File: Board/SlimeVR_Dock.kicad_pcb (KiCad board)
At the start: 2 copper layers, 83.8 x 76.8 mm, 91 parts, among them J1_Control1 Conn_01x03_Pin, J1_MainPW1 USB_C_Receptacle_USB2.0_16P, J1_Monitor1 Conn_01x03_Pin, J1_Prog1 Conn_01x03_Pin, J2 USB_C_Receptacle_USB2.0_16P, J3 USB_C_Receptacle_USB2.0_16P, J4 USB_C_Receptacle_USB2.0_16P, J5 USB_C_Receptacle_USB2.0_16P, J6 USB_C_Receptacle_USB2.0_16P, J7 USB_C_Receptacle_USB2.0_16P, J8 USB_C_Receptacle_USB2.0_16P, J9 USB_C_Receptacle_USB2.0_16P, Q1 AO3401A, Q2 BC857, Q3 BC857, Q4 BC857, Q5 BC857, U1 ESP32-C3-WROOM-02, U10 INA226, U11 AP22652W6-7, U12 INA226, U13 INA226, U14 AP22652W6-7, U15 INA226, U16 INA226, U17 74HC165, U18 74HC165, U19 74HC595, U2 CH224K, U3 XC6220B331MR, U5 AP22652W6-7, U6 INA226, U7 INA226, U8 AP22652W6-7, U9 INA226

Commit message: Updavení USB-C
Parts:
- removed JFan1: Conn_01x04_Pin, Connector:FanPinHeader_1x04_P2.54mm_Vertical
- added BZ1: Buzzer, Buzzer_Beeper:Buzzer_12x9.5RM7.6, F.Cu at (121.4, 72.0)
- added D1: 1N4148, Diode_SMD:D_0603_1608Metric, F.Cu at (134.4, 61.8)
- added J1Fan1: Conn_01x04_Pin, Connector:FanPinHeader_1x04_P2.54mm_Vertical, F.Cu at (124.9, 42.4)
- added J1Temp1: Conn_01x05_Pin, Connector_PinHeader_2.54mm:PinHeader_1x05_P2.54mm_Vertical, F.Cu at (124.9, 49.0)
- added Q6: BC817, Package_TO_SOT_SMD:SOT-23, F.Cu at (134.4, 72.2)
- added R33: 1k, Resistor_SMD:R_0603_1608Metric, F.Cu at (103.1, 85.6)
- moved J_FromR0 65.2 mm to (129.5, 49.0)
- moved J_ToR0 65.2 mm to (134.1, 49.0)
- moved U2 53.6 mm to (131.4, 57.3)
- moved C19 43.3 mm to (163.4, 61.8)
- moved R32 43.3 mm to (163.4, 78.7)
- moved C14 43.3 mm to (163.4, 47.3)
- moved C21 43.3 mm to (163.4, 76.2)
- moved J2 43.3 mm to (161.5, 43.2)
- moved J6 43.3 mm to (161.5, 57.6)
- moved R25 43.3 mm to (163.4, 49.8)
- moved R30 43.3 mm to (163.4, 64.3)
- moved U12 43.3 mm to (157.7, 62.8)
- moved U6 43.3 mm to (157.7, 48.4)
- moved J8 43.3 mm to (161.5, 72.1)
- moved U15 43.3 mm to (157.7, 77.2)
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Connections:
- U19 pad 4: unconnected-(U19-QE-Pad4) -> BZ
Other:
- board size 83.8 x 76.8 mm -> 82.8 x 69.8 mm

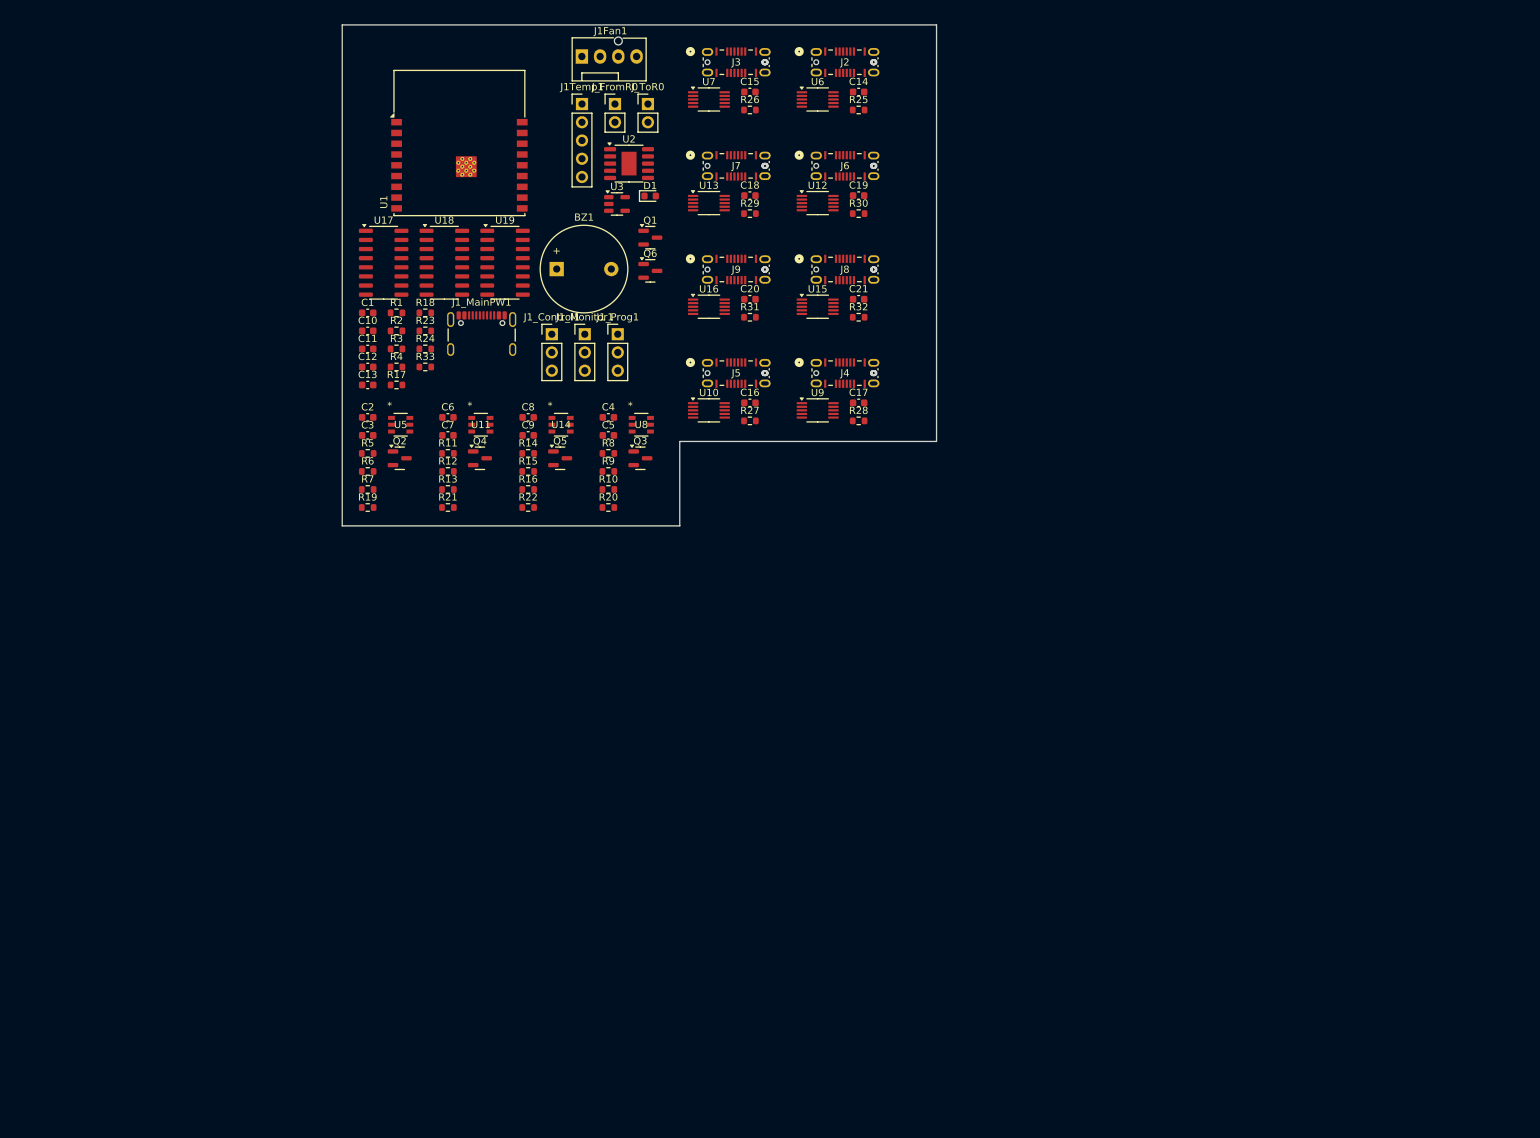
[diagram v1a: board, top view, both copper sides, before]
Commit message: layout
-bude asi potreba jiny footrpint usb-c
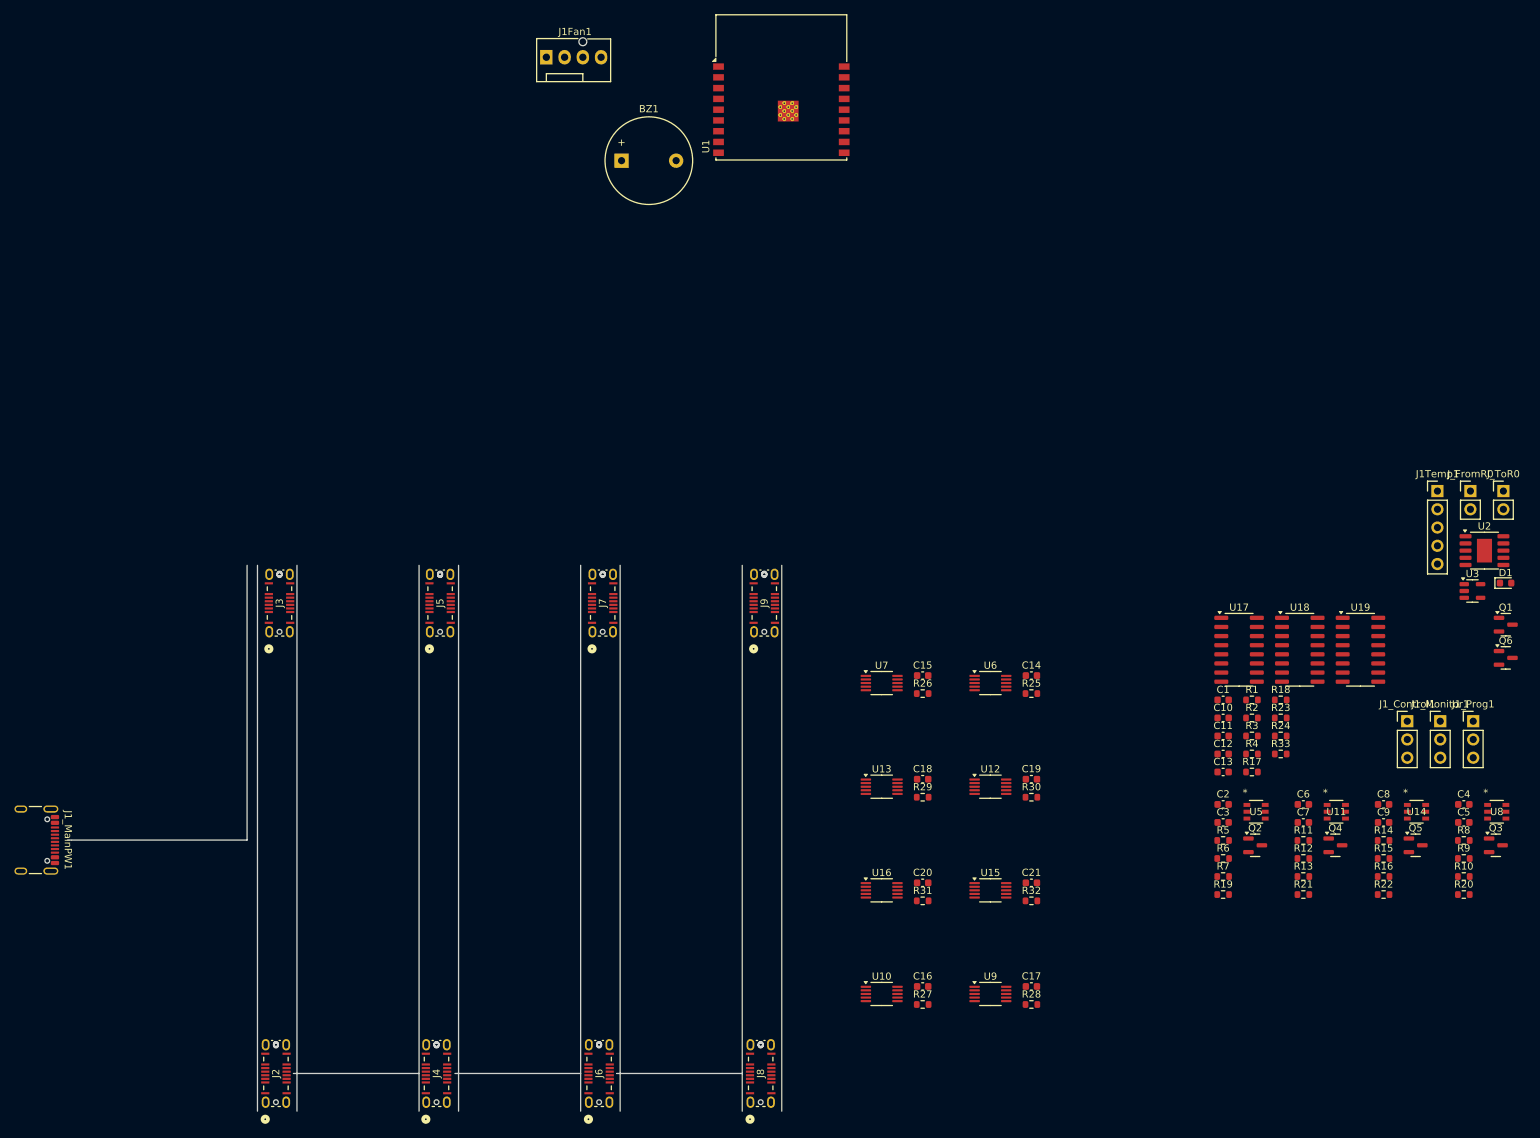
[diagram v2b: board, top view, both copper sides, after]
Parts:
- moved J2 161.6 mm to (82.3, 184.0), turned to 90 degrees
- moved J6 130.9 mm to (127.3, 184.0), turned to 90 degrees
- moved Q2 130.7 mm to (218.6, 152.2)
- moved Q5 130.7 mm to (241.0, 152.2)
- moved R18 130.7 mm to (222.2, 132.0)
- moved R23 130.7 mm to (222.2, 134.5)
- moved R24 130.7 mm to (222.2, 137.0)
- moved R33 130.7 mm to (222.2, 139.5)
- moved C1 130.7 mm to (214.2, 132.0)
- moved C10 130.7 mm to (214.2, 134.5)
- moved C11 130.7 mm to (214.2, 137.0)
- moved C12 130.7 mm to (214.2, 139.5)
- moved C13 130.7 mm to (214.2, 142.0)
- moved C2 130.7 mm to (214.2, 146.5)
- moved C3 130.7 mm to (214.2, 149.0)
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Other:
- board size 82.8 x 69.8 mm -> 99.4 x 76 mm

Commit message: minority upravy
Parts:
- added C22: 10uF, Capacitor_SMD:C_1210_3225Metric, F.Cu at (221.4, 37.4)
- added C23: 10uF, Capacitor_SMD:C_1210_3225Metric, F.Cu at (221.4, 41.6)
- added C24: 47uF, Capacitor_SMD:C_0805_2012Metric, F.Cu at (216.3, 36.8)
- added C25: 47uF, Capacitor_SMD:C_0805_2012Metric, F.Cu at (216.3, 39.8)
- added C26: 47uF, Capacitor_SMD:C_0805_2012Metric, F.Cu at (216.3, 42.8)
- added C27: 100nF, Capacitor_SMD:C_0805_2012Metric, F.Cu at (216.3, 45.8)
- added C28: 100nF, Capacitor_SMD:C_0805_2012Metric, F.Cu at (216.3, 48.8)
- added C29: 4.7uF, Capacitor_SMD:C_0805_2012Metric, F.Cu at (216.3, 51.8)
- added C30: 10uF, Capacitor_SMD:C_1210_3225Metric, F.Cu at (221.4, 45.9)
- added L1: 2.2uH, Inductor_SMD:L_Vishay_IHLP-2525, F.Cu at (223.5, 52.0)
- added R34: 10k, Resistor_SMD:R_0603_1608Metric, F.Cu at (212.1, 36.5)
- added R35: 1.4k, Resistor_SMD:R_0603_1608Metric, F.Cu at (212.1, 39.0)
- added R36: 100k, Resistor_SMD:R_0603_1608Metric, F.Cu at (212.1, 41.5)
- added R37: 100k, Resistor_SMD:R_0603_1608Metric, F.Cu at (212.1, 44.1)
- added R38: 1, Resistor_SMD:R_0603_1608Metric, F.Cu at (212.1, 46.6)
- added R39: 43k, Resistor_SMD:R_0603_1608Metric, F.Cu at (212.1, 49.1)
- added R40: 240k, Resistor_SMD:R_0603_1608Metric, F.Cu at (212.1, 51.6)
- added R41: 75k, Resistor_SMD:R_0603_1608Metric, F.Cu at (212.1, 54.1)
- added U4: TPS548A20RVER, Library:RVE0028A, F.Cu at (230.6, 39.1)
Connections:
- BZ1 pad 1: +5V -> 5VStepDwon
- C10 pad 1: +5V -> 5VStepDwon
- C11 pad 1: +5V -> 5VStepDwon
- C2 pad 1: +5V -> 5VStepDwon
- C4 pad 1: +5V -> 5VStepDwon
- C6 pad 1: +5V -> 5VStepDwon
- C8 pad 1: +5V -> 5VStepDwon
- D1 pad 1: +5V -> 5VStepDwon
- J1Fan1 pad 2: +5V -> 5VStepDwon
- Q1 pad 3: Net-(J_ToR0-Pin_2) -> /StepDown/Vin
- R4 pad 2: Net-(J_ToR0-Pin_2) -> /StepDown/Vin
- U11 pad 1: +5V -> 5VStepDwon
- U14 pad 1: +5V -> 5VStepDwon
- U19 pad 10: +5V -> 5VStepDwon
- U3 pad 1: +5V -> 5VStepDwon
- U3 pad 3: +5V -> 5VStepDwon
- U5 pad 1: +5V -> 5VStepDwon
- U8 pad 1: +5V -> 5VStepDwon

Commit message: pcb layout
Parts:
- removed J_FromR0, J_ToR0: Conn_01x02_Pin, Connector_PinHeader_2.54mm:PinHeader_1x02_P2.54mm_Vertical
- C14, C15, C16, C17, C18, C19, C2, C20, C21, C28, C29, C3, C4, C5, C6, C7, C8, C9, D1, J1Temp1, Q2, Q3, Q4, Q5, Q6, R10, R11, R12, R13, R14, R15, R16, R17, R18, R19, R20, R21, R22, R23, R24, R25, R26, R27, R28, R29, R30, R31, R32, R33, R38, R40, R41, R5, R6, R7, R8, R9, U1, U10, U11, U12, U13, U14, U15, U16, U17, U18, U19, U5, U6, U7, U8, U9: moved to B.Cu
- Q1: value AO3401A -> NDT452AP; footprint Package_TO_SOT_SMD:SOT-23 -> Package_TO_SOT_SMD:SOT-223
- moved J1Temp1 220.3 mm to (28.0, 146.0), turned to 90 degrees
- moved J1_Control1 218.4 mm to (21.4, 135.0)
- moved J1_Monitor1 218.4 mm to (26.0, 135.0)
- moved J1_Prog1 218.4 mm to (30.6, 135.0)
- moved C28 207.0 mm to (40.0, 157.0), turned to 180 degrees
- moved C29 207.0 mm to (40.0, 160.1), turned to 180 degrees
- moved C22 201.0 mm to (58.7, 155.4), turned to 180 degrees
- moved R18 200.1 mm to (26.8, 175.0), turned to 180 degrees
- moved R23 200.1 mm to (26.8, 177.5), turned to 180 degrees
- moved R24 200.1 mm to (26.8, 180.0), turned to 180 degrees
- moved U4 198.6 mm to (64.4, 147.9), turned to 180 degrees
- moved Q1 198.0 mm to (57.1, 146.8)
- moved U2 197.3 mm to (59.6, 161.0), turned to 180 degrees
- moved C23 196.6 mm to (58.7, 152.1), turned to 180 degrees
- moved D1 195.9 mm to (69.3, 182.4), turned to 90 degrees
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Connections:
- Q1 pad 2: VBUS -> /StepDown/Vin
- Q1 pad 3: /StepDown/Vin -> VBUS
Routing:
- net Net-(U2-DM): track 0.00 -> 37.4 mm, vias 0 -> 2
- net Net-(U2-DP): track 0.00 -> 36.6 mm, vias 0 -> 4
- net Net-(Q1-G): track 0.00 -> 22.1 mm, vias 0 -> 2
- net VBUS: track 0.00 -> 19.3 mm
- net Net-(J1_MainPW1-CC1): track 0.00 -> 18.4 mm, vias 0 -> 2
- net 5VStepDwon: track 0.00 -> 13.4 mm
- net Net-(J1_MainPW1-CC2): track 0.00 -> 13.3 mm, vias 0 -> 2
- net /StepDown/Vin: track 0.00 -> 10.8 mm, vias 0 -> 2
- net Net-(U4-MODE): track 0.00 -> 7.57 mm
- net Net-(U4-FB): track 0.00 -> 5.72 mm
- net Net-(U2-CFG2): track 0.00 -> 4.68 mm
- net Net-(U4-VBST): track 0.00 -> 3.66 mm
- net +3V3: track 0.00 -> 3.16 mm
- net Net-(U4-TRIP): track 0.00 -> 3.06 mm
- net Net-(U2-VBUS): track 0.00 -> 2.17 mm
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- added copper zone on F.Cu, net /StepDown/Vin
- added copper zone on F.Cu, net 5VStepDwon
- added copper zone on F.Cu, net Net-(C27-Pad2)
- added copper zone on F.Cu, net VBUS
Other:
- board size 99.4 x 76 mm -> 163.1 x 106 mm

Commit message: upraveni veliskoti
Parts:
- C28, C29, J1Temp1, R23, R24, R38, R40, R41: moved to F.Cu
- moved R23 135.9 mm to (114.8, 74.0)
- moved R24 130.3 mm to (104.6, 75.5)
- moved R17 104.9 mm to (114.2, 121.5), turned to 0 degrees
- moved R18 99.6 mm to (110.8, 121.5)
- moved C29 99.4 mm to (120.9, 102.3), turned to 0 degrees
- moved C28 91.9 mm to (112.6, 100.7), turned to -90 degrees
- moved J1_Prog1 90.9 mm to (97.9, 74.0)
- moved J1_Control1 90.0 mm to (110.0, 119.0), turned to 90 degrees
- moved J1_Monitor1 88.9 mm to (98.0, 82.9)
- moved J1Temp1 82.8 mm to (104.9, 115.3)
- moved J1Fan1 80.7 mm to (99.9, 110.3), turned to -90 degrees
- moved C15 75.7 mm to (133.3, 74.9)
- moved R26 75.7 mm to (133.3, 77.4)
- moved R37 75.0 mm to (120.7, 96.3), turned to 0 degrees
- moved R36 74.4 mm to (114.4, 99.8), turned to 90 degrees
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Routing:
- net +3V3: track 3.16 -> 47.0 mm, vias 0 -> 1
- net Net-(U4-VREG): track 0.00 -> 17.3 mm
- net RX: track 0.00 -> 7.94 mm
- net TX: track 0.00 -> 6.90 mm
- net Net-(U4-VDD): track 0.00 -> 6.23 mm
- net Net-(U4-RF): track 0.00 -> 5.05 mm
- net Net-(U4-MODE): track 7.57 -> 3.79 mm
- net D-: track 0.00 -> 3.51 mm
- net D+: track 0.00 -> 3.50 mm
- net /StepDown/Vin: track 10.8 -> 12.3 mm
- net Net-(U4-TRIP): track 3.06 -> 4.49 mm
- net Net-(U4-FB): track 5.72 -> 6.72 mm
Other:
- board size 163.1 x 106 mm -> 100 x 78.3 mm

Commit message: prvni segment usb-c
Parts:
- moved U17 89.8 mm to (265.2, 99.2)
- moved U18 89.8 mm to (243.2, 99.2)
- moved U19 89.8 mm to (219.7, 99.4)
- moved C4 83.7 mm to (229.2, 128.8)
- moved C5 83.7 mm to (229.2, 131.3)
- moved C6 83.7 mm to (251.9, 128.8)
- moved C7 83.7 mm to (251.9, 131.3)
- moved C8 83.7 mm to (268.1, 128.7)
- moved C9 83.7 mm to (268.1, 131.2)
- moved Q3 83.7 mm to (224.7, 134.5)
- moved Q4 83.7 mm to (247.4, 134.5)
- moved R10 83.7 mm to (229.2, 138.8)
- moved R11 83.7 mm to (251.9, 133.8)
- moved R12 83.7 mm to (251.9, 136.3)
- moved R13 83.7 mm to (251.9, 138.8)
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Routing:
- net +3V3: track 47.0 -> 187.2 mm
- net /Dual_USB-C_SubSchema0/USB_C0/CC_Line: track 0.00 -> 56.8 mm, vias 0 -> 2
- net /Dual_USB-C_SubSchema0/USB_C0/VBUS: track 0.00 -> 46.0 mm, vias 0 -> 2
- net Net-(U6-Vin-): track 0.00 -> 19.1 mm, vias 0 -> 1
- net Net-(U7-Vin-): track 0.00 -> 13.6 mm, vias 0 -> 1
- net 5VStepDwon: track 13.7 -> 17.9 mm, vias 0 -> 1
- net Alert01: track 0.00 -> 2.80 mm
- net Alert00: track 0.00 -> 2.47 mm
- net Net-(U5-ILIM): track 0.00 -> 1.82 mm
- net CC0: track 0.00 -> 1.65 mm
- net /StepDown/Vin: track 12.3 -> 11.5 mm
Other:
- outline, holes or cut-outs redrawn

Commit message: pokus o posunutí cívky
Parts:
- moved C24 5.63 mm to (115.3, 80.9)
- moved C25 5.63 mm to (113.3, 80.9)
- moved C26 5.63 mm to (111.3, 80.9)
- moved L1 3.49 mm to (114.3, 87.0), turned to 0 degrees
- moved C27 2.00 mm to (119.9, 92.5)
- moved C30 0.92 mm to (108.2, 88.2), turned to 90 degrees
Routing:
- net +3V3: track 187.2 -> 189.8 mm
- net 5VStepDwon: track 17.9 -> 15.4 mm
- net Net-(U4-VBST): track 3.66 -> 5.37 mm

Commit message: almost finished layout V1
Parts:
- C28, C29, R34, R35, R36, R37, R38, R39, R40, R41: moved to B.Cu
- moved U17 128.6 mm to (136.7, 104.9), turned to -90 degrees
- moved R21 99.4 mm to (174.2, 79.3)
- moved R11 98.6 mm to (163.0, 91.2), turned to 90 degrees
- moved R20 97.6 mm to (153.8, 79.3)
- moved R8 96.1 mm to (143.0, 91.2), turned to 90 degrees
- moved Q4 92.5 mm to (164.4, 93.7), turned to 90 degrees
- moved R13 92.1 mm to (162.2, 117.6), turned to 0 degrees
- moved R12 91.9 mm to (168.4, 97.8), turned to -90 degrees
- moved C6 91.8 mm to (168.1, 91.2), turned to 0 degrees
- moved C7 91.4 mm to (166.8, 97.8), turned to -90 degrees
- moved Q3 90.0 mm to (144.4, 93.7), turned to 90 degrees
- moved C4 89.5 mm to (148.0, 91.1), turned to 0 degrees
- moved R9 89.4 mm to (148.5, 97.7), turned to -90 degrees
- moved R10 89.4 mm to (142.3, 117.6), turned to 0 degrees
- moved C5 88.8 mm to (146.9, 97.7), turned to -90 degrees
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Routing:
- net SDA: track 0.00 -> 222.4 mm, vias 0 -> 5
- net +3V3: track 189.8 -> 392.8 mm, vias 1 -> 20
- net SCL: track 0.00 -> 196.7 mm, vias 0 -> 4
- net CLK: track 0.00 -> 179.7 mm, vias 0 -> 8
- net GET: track 0.00 -> 162.7 mm, vias 0 -> 10
- net Data_Out: track 0.00 -> 131.8 mm, vias 0 -> 2
- net Data_In: track 0.00 -> 99.5 mm, vias 0 -> 4
- net 5VStepDwon: track 15.4 -> 93.8 mm, vias 1 -> 7
- net Enable: track 0.00 -> 73.6 mm, vias 0 -> 2
- net Boot: track 0.00 -> 60.6 mm, vias 0 -> 2
- net Net-(U17-~{Q7}): track 0.00 -> 58.3 mm, vias 0 -> 6
- net TACH: track 0.00 -> 57.3 mm
- net /Dual_USB-C_SubSchema1/USB_C0/VBUS: track 0.00 -> 53.9 mm, vias 0 -> 2
- net PWM: track 0.00 -> 53.7 mm
- net /Dual_USB-C_SubSchema2/USB_C0/CC_Line: track 0.00 -> 52.3 mm, vias 0 -> 2
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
